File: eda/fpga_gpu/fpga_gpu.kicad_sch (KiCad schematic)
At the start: 25 parts, among them U1 ICE40HX4K-TQ144, U2 SST25VF080B-50-4x-S2Ax, U8 AMS1117-3.3, U9 AP2112K-1.2, X1 TXC-7C

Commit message: GPU routing
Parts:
- added U10: IS61C5128AL-10KLI, Package_SO:SOJ-36_10.16x23.49mm_P1.27mm, symbol Memory_RAM:IS61C5128AL-10KLI
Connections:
- net ADev0: now also U1.114 (IOT_171); no longer U1.110 (IOT_168)
- net ADev1: now also U1.113 (IOT_170); no longer U1.112 (IOT_169)
- net ADev2: now also U1.112 (IOT_169); no longer U1.113 (IOT_170)
- net ADev3: now also U1.110 (IOT_168); no longer U1.114 (IOT_171)
- net GND: now also U10.10 (GND), U10.28 (GND)
- new net: U10.27 (VDD), U10.9 (VDD)
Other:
- moved on the sheet: C10, C2, C3, C4, C5, C6, C7, C8, C9, D1, R1, R2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

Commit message: More routing on the GPU board
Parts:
- added C23: 100n, Capacitor_SMD:C_0805_2012Metric, symbol Device:C
- added H1, H2, H3, H4: MountingHole, MountingHole:MountingHole_2.5mm, symbol Mechanical:MountingHole
- added J3: programming, Connector_PinHeader_2.54mm:PinHeader_1x06_P2.54mm_Vertical, symbol Connector:Conn_01x06_Pin
- added J4: reset ground, Connector_PinHeader_2.54mm:PinHeader_1x01_P2.54mm_Vertical, symbol Connector:Conn_01x01_Pin
- added Q1: 2N7002, Package_TO_SOT_SMD:SOT-23, symbol Transistor_FET:2N7002
- added R15, R16: 10k, Resistor_SMD:R_0805_2012Metric, symbol Device:R
- D1: footprint Diode_THT:D_DO-41_SOD81_P10.16mm_Horizontal -> Diode_SMD:D_0805_2012Metric
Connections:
- net +3.3V: now also R16.2
- net Blue0: now also U1.78 (IOR_114); no longer U1.37 (IOB_56)
- net Blue1: now also U1.79 (IOR_115); no longer U1.38 (IOB_57)
- net Blue2: now also U1.80 (IOR_116); no longer U1.39 (IOB_61)
- net DIn0: now also U1.88 (IOR_137); no longer U1.73 (IOR_109)
- net DIn1: now also U1.90 (IOR_138); no longer U1.74 (IOR_110)
- net DIn2: now also U1.91 (IOR_139); no longer U1.75 (IOR_111)
- net DIn3: now also U1.93 (IOR_140_GBIN3); no longer U1.76 (IOR_112)
- net DIn4: now also U1.94 (IOR_141_GBIN2); no longer U1.78 (IOR_114)
- net DIn5: now also U1.95 (IOR_144); no longer U1.79 (IOR_115)
- net DIn6: now also U1.96 (IOR_146); no longer U1.80 (IOR_116)
- net DIn7: now also U1.97 (IOR_147); no longer U1.81 (IOR_117)
- net DOut0: now also U1.98 (IOR_148); no longer U1.82 (IOR_118)
- net DOut1: now also U1.99 (IOR_152); no longer U1.83 (IOR_119)
- net DOut2: now also U1.101 (IOR_160); no longer U1.84 (IOR_120)
- net DOut3: now also U1.102 (IOR_161); no longer U1.85 (IOR_128)
- net DOut4: now also U1.104 (IOR_164); no longer U1.87 (IOR_136)
- net DOut5: now also U1.105 (IOR_165); no longer U1.88 (IOR_137)
- net DOut6: now also U1.106 (IOR_166); no longer U1.90 (IOR_138)
- net DOut7: now also U1.107 (IOR_167); no longer U1.91 (IOR_139)
- net GND: now also C23.2, J3.2 (Pin_2), J4.1 (Pin_1), Q1.2 (S), R15.1
- net Green0: now also U1.81 (IOR_117); no longer U1.41 (IOB_63)
- net Green1: now also U1.82 (IOR_118); no longer U1.42 (IOB_64)
- net Green2: now also U1.83 (IOR_119); no longer U1.43 (IOB_71)
- net HSYNC: now also U1.75 (IOR_111); no longer U1.55 (IOB_91)
- net Red0: now also U1.84 (IOR_120); no longer U1.44 (IOB_72)
- net Red1: now also U1.85 (IOR_128); no longer U1.45 (IOB_73)
- net Red2: now also U1.87 (IOR_136); no longer U1.47 (IOB_79)
- net VCC: now also U10.27 (VDD), U10.9 (VDD), C23.1
- net VSYNC: now also U1.76 (IOR_112); no longer U1.48 (IOB_80)
- net ice40-CRESET: now also J3.1 (Pin_1), R16.1
- net ice40-SCK: now also J3.5 (Pin_5)
- net ice40-SDI: now also J3.3 (Pin_3)
- net ice40-SDO: now also J3.4 (Pin_4)
- net at R1.2, R4.2, U2.1 (~{CE}): now also J3.6 (Pin_6)
- net RamA0: now reaches U10.1 (A0)
- net RamA0: now also U1.18 (IOL_12B)
- net RamIo2: now reaches U10.11 (I/O2)
- net RamIo2: now also U1.63 (IOB_103_CBSEL0)
- net RamIo3: now reaches U10.12 (I/O3)
- net RamIo3: now also U1.64 (IOB_104_CBSEL1)
- net ~{RamWE}: now reaches U10.13 (~{WE})
- net ~{RamWE}: now also U1.44 (IOB_72)
- net RamA5: now reaches U10.14 (A5)
- net RamA5: now also U1.11 (IOL_8A)
- net RamA6: now reaches U10.15 (A6)
- net RamA6: now also U1.10 (IOL_5B)
- net RamA7: now reaches U10.16 (A7)
- net RamA7: now also U1.9 (IOL_5A)
- net RamA8: now reaches U10.17 (A8)
- net RamA8: now also U1.8 (IOL_4B)
- net RamA9: now reaches U10.18 (A9)
- net RamA9: now also U1.7 (IOL_4A)
- net RamA1: now reaches U10.2 (A1)
- net RamA1: now also U1.17 (IOL_12A)
- net RamA10: now reaches U10.20 (A10)
- net RamA10: now also U1.19 (IOL_13A)
- net RamA11: now reaches U10.21 (A11)
- net RamA11: now also U1.21 (IOL_14A_GBIN6)
- net RamA12: now reaches U10.22 (A12)
- net RamA12: now also U1.22 (IOL_14B)
- net RamA13: now reaches U10.23 (A13)
- net RamA13: now also U1.23 (IOL_17A)
- net RamA14: now reaches U10.24 (A14)
- net RamA14: now also U1.24 (IOL_17B)
- net RamIo4: now reaches U10.25 (I/O4)
- net RamIo4: now also U1.60 (IOB_95)
- net RamIo5: now reaches U10.26 (I/O5)
- net RamIo5: now also U1.56 (IOB_94)
- net RamIo6: now reaches U10.29 (I/O6)
- net RamIo6: now also U1.55 (IOB_91)
- net RamA2: now reaches U10.3 (A2)
- net RamA2: now also U1.16 (IOL_10B)
- net RamIo7: now reaches U10.30 (I/O7)
- net RamIo7: now also U1.52 (IOB_82_GBIN4)
- net ~{RamOE}: now reaches U10.31 (~{OE})
- net ~{RamOE}: now also U1.45 (IOB_73)
- net RamA15: now reaches U10.32 (A15)
- net RamA15: now also U1.25 (IOL_18A)
- net RamA16: now reaches U10.33 (A16)
- net RamA16: now also U1.29 (IOL_23B)
- net RamA17: now reaches U10.34 (A17)
- net RamA17: now also U1.31 (IOL_24A)
- net RamA18: now reaches U10.35 (A18)
- net RamA18: now also U1.32 (IOL_24B)
- net RamA3: now reaches U10.4 (A3)
- net RamA3: now also U1.15 (IOL_10A)
- net RamA4: now reaches U10.5 (A4)
- net RamA4: now also U1.12 (IOL_8B)
- net ~{RamCE}: now reaches U10.6 (~{CE})
- net ~{RamCE}: now also U1.43 (IOB_71)
- net RamIo0: now reaches U10.7 (I/O0)
- net RamIo0: now also U1.61 (IOB_96)
- net RamIo1: now reaches U10.8 (I/O1)
- net RamIo1: now also U1.62 (IOB_102)
- net FpgaIRQ: now reaches U1.128 (IOT_197_GBIN1)
- net FpgaIRQ: now also Q1.1 (G), R15.2
- new net Interfacing/~{IRQ}: Q1.3 (D)
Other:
- sheet Interfacing ports: added ~{IRQ}; removed none
- moved on the sheet: C1, C10, C19, C2, C20, C21, C22, C3, C4, C5, C6, C7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

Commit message: Update eda
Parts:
- added SW1: SW_Reset, Button_Switch_SMD:SW_SPST_TL3305A, symbol Switch:SW_Push
- added SW2: SW_FlashPwrCycle, Button_Switch_SMD:SW_SPST_TL3305A, symbol Switch:SW_Push_Open
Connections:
- net +3.3V: now also SW2.2 (B); no longer R2.2, R3.2, U2.8 (VDD)
- net GND: now also SW1.1
- net ice40-CRESET: now also SW1.2
- new net: R2.2, R3.2, SW2.1 (A), U2.8 (VDD)
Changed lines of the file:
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@@
   (junction (at 302.26 214.63) (diameter 0) (color 0 0 0 0)
   )
+  (junction (at 210.82 266.7) (diameter 0) (color 0 0 0 0)
+  )
   (junction (at 142.24 209.55) (diameter 0) (color 0 0 0 0)
   )
@@
   (junction (at 201.93 86.36) (diameter 0) (color 0 0 0 0)
   )
+  (junction (at 226.06 278.765) (diameter 0) (color 0 0 0 0)
+  )
   (junction (at 350.52 142.24) (diameter 0) (color 0 0 0 0)
   )
@@
     (stroke (width 0) (type default))
   )
+  (wire (pts (xy 232.41 194.945) (xy 232.41 196.85))
+    (stroke (width 0) (type default))
+  )
   (wire (pts (xy 350.52 71.12) (xy 386.08 71.12))
     (stroke (width 0) (type default))
@@
     (stroke (width 0) (type default))
   )
+  (wire (pts (xy 210.82 278.765) (xy 226.06 278.765))
+    (stroke (width 0) (type default))
+  )
   (wire (pts (xy 26.67 239.395) (xy 29.845 239.395))
     (stroke (width 0) (type default))
@@
     (stroke (width 0) (type default))
   )
-  (wire (pts (xy 226.06 271.78) (xy 226.06 274.32))
+  (wire (pts (xy 226.06 271.78) (xy 226.06 278.765))
     (stroke (width 0) (type default))
   )
@@
     (stroke (width 0) (type default))
   )
-  (wire (pts (xy 201.93 266.7) (xy 228.6 266.7))
+  (wire (pts (xy 201.93 266.7) (xy 210.82 266.7))
     (stroke (width 0) (type default))
   )
@@
     (stroke (width 0) (type default))
   )
+  (wire (pts (xy 210.82 266.7) (xy 228.6 266.7))
+    (stroke (width 0) (type default))
+  )
   (wire (pts (xy 56.515 252.73) (xy 56.515 251.46))
     (stroke (width 0) (type default))
@@
     (stroke (width 0) (type default))
   )
+  (wire (pts (xy 226.06 278.765) (xy 226.06 280.035))
+    (stroke (width 0) (type default))
+  )
   (wire (pts (xy 137.16 217.17) (xy 134.62 217.17))
     (stroke (width 0) (type default))
@@
     (stroke (width 0) (type default))
   )
+  (wire (pts (xy 210.82 276.86) (xy 210.82 278.765))
+    (stroke (width 0) (type default))
+  )
   (wire (pts (xy 200.66 220.98) (xy 201.93 220.98))
     (stroke (width 0) (type default))
@@
     )
   )
-  (symbol (lib_id "power:GND") (at 226.06 274.32 0) (unit 1)
-    (in_bom yes) (on_board yes) (dnp no) (fields_autoplaced)
-    (property "Reference" "#PWR046" (at 226.06 280.67 0)
+  (symbol (lib_id "power:GND") (at 226.06 280.035 0) (unit 1)
+    (in_bom yes) (on_board yes) (dnp no)
+    (property "Reference" "#PWR046" (at 226.06 286.385 0)
       (effects (font (size 1.27 1.27)) hide)
     )
-    (property "Value" "GND" (at 226.06 279.4 0)
+    (property "Value" "GND" (at 226.06 283.845 0)
       (effects (font (size 1.27 1.27)))
     )
-    (property "Footprint" "" (at 226.06 274.32 0)
+    (property "Footprint" "" (at 226.06 280.035 0)
       (effects (font (size 1.27 1.27)) hide)
     )
-    (property "Datasheet" "" (at 226.06 274.32 0)
+    (property "Datasheet" "" (at 226.06 280.035 0)
       (effects (font (size 1.27 1.27)) hide)
     )
@@
     )
   )
+  (symbol (lib_id "Switch:SW_Push") (at 210.82 271.78 90) (unit 1)
+    (in_bom yes) (on_board yes) (dnp no) (fields_autoplaced)
+    (property "Reference" "SW1" (at 212.09 271.145 90)
+      (effects (font (size 1.27 1.27)) (justify right))
+    )
+    (property "Value" "SW_Reset" (at 212.09 273.685 90)
+      (effects (font (size 1.27 1.27)) (justify right))
+    )
+    (property "Footprint" "Button_Switch_SMD:SW_SPST_TL3305A" (at 205.74 271.78 0)
+      (effects (font (size 1.27 1.27)) hide)
+    )
+    (property "Datasheet" "~" (at 205.74 271.78 0)
+      (effects (font (size 1.27 1.27)) hide)
+    )
+    (pin "1")
+    (pin "2")
+    (instances
+      (project "fpga_gpu"
+        (path "/1109c9a4-a9ef-4407-8781-29fe7740bcaf"
+          (reference "SW1") (unit 1)
+        )
+      )
+    )
+  )
   (symbol (lib_id "power:GND") (at 165.1 220.98 0) (unit 1)
     (in_bom yes) (on_board yes) (dnp no) (fields_autoplaced)
@@
     )
   )
-  (symbol (lib_id "power:+3.3V") (at 232.41 207.01 0) (unit 1)
+  (symbol (lib_id "power:+3.3V") (at 232.41 194.945 0) (unit 1)
     (in_bom yes) (on_board yes) (dnp no) (fields_autoplaced)
-    (property "Reference" "#PWR014" (at 232.41 210.82 0)
+    (property "Reference" "#PWR014" (at 232.41 198.755 0)
       (effects (font (size 1.27 1.27)) hide)
     )
-    (property "Value" "+3.3V" (at 232.41 203.2 0)
+    (property "Value" "+3.3V" (at 232.41 191.135 0)
       (effects (font (size 1.27 1.27)))
     )
-    (property "Footprint" "" (at 232.41 207.01 0)
+    (property "Footprint" "" (at 232.41 194.945 0)
       (effects (font (size 1.27 1.27)) hide)
     )
-    (property "Datasheet" "" (at 232.41 207.01 0)
+    (property "Datasheet" "" (at 232.41 194.945 0)
       (effects (font (size 1.27 1.27)) hide)
     )
@@
         )
       )
+    )
+  )
+  (symbol (lib_id "Switch:SW_Push_Open") (at 232.41 201.93 90) (unit 1)
+    (in_bom yes) (on_board yes) (dnp no) (fields_autoplaced)
+    (property "Reference" "SW2" (at 233.68 201.295 90)
+      (effects (font (size 1.27 1.27)) (justify right))
+    )
+    (property "Value" "SW_FlashPwrCycle" (at 233.68 203.835 90)
+      (effects (font (size 1.27 1.27)) (justify right))
+    )
+    (property "Footprint" "Button_Switch_SMD:SW_SPST_TL3305A" (at 227.33 201.93 0)
+      (effects (font (size 1.27 1.27)) hide)
+    )
+    (property "Datasheet" "~" (at 227.33 201.93 0)
+      (effects (font (size 1.27 1.27)) hide)
+    )
+    (pin "1")
+    (pin "2")
+    (instances
+      (project "fpga_gpu"
+        (path "/1109c9a4-a9ef-4407-8781-29fe7740bcaf"
+          (reference "SW2") (unit 1)
+        )
+      )

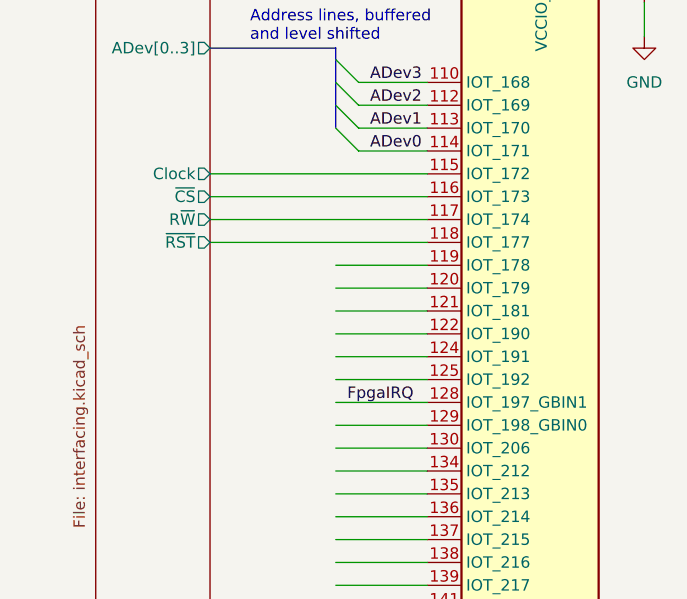
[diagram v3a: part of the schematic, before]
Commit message: Add skeleton stuff to io-card and gpu
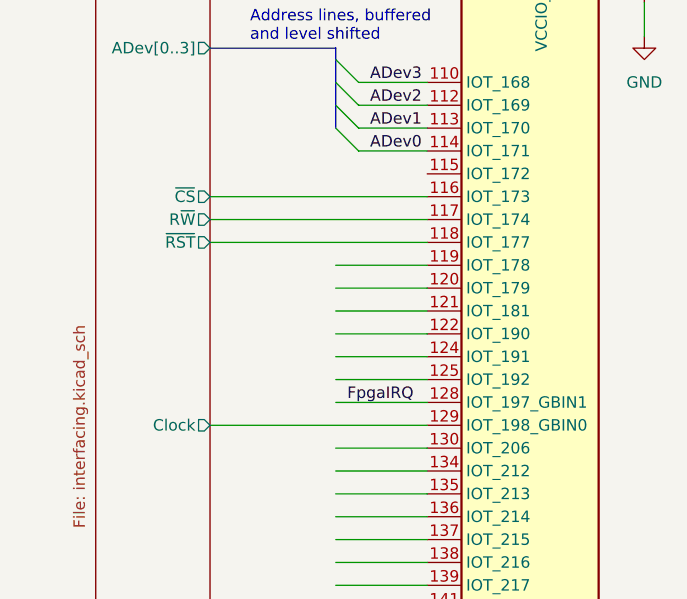
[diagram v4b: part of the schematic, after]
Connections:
- net Interfacing/Clock: now also U1.129 (IOT_198_GBIN0); no longer U1.115 (IOT_172)
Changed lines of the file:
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@@
     (stroke (width 0) (type default))
   )
-  (wire (pts (xy 59.69 119.38) (xy 69.85 119.38))
-    (stroke (width 0) (type default))
-  )
   (wire (pts (xy 264.16 88.9) (xy 274.32 88.9))
     (stroke (width 0) (type default))
@@
     (stroke (width 0) (type default))
   )
-  (wire (pts (xy 45.72 91.44) (xy 69.85 91.44))
+  (wire (pts (xy 45.72 119.38) (xy 69.85 119.38))
     (stroke (width 0) (type default))
   )
@@
       (effects (font (size 1.27 1.27)) (justify right))
     )
-    (pin "Clock" output (at 45.72 91.44 0)
+    (pin "Clock" output (at 45.72 119.38 0)
       (effects (font (size 1.27 1.27)) (justify right))
     )

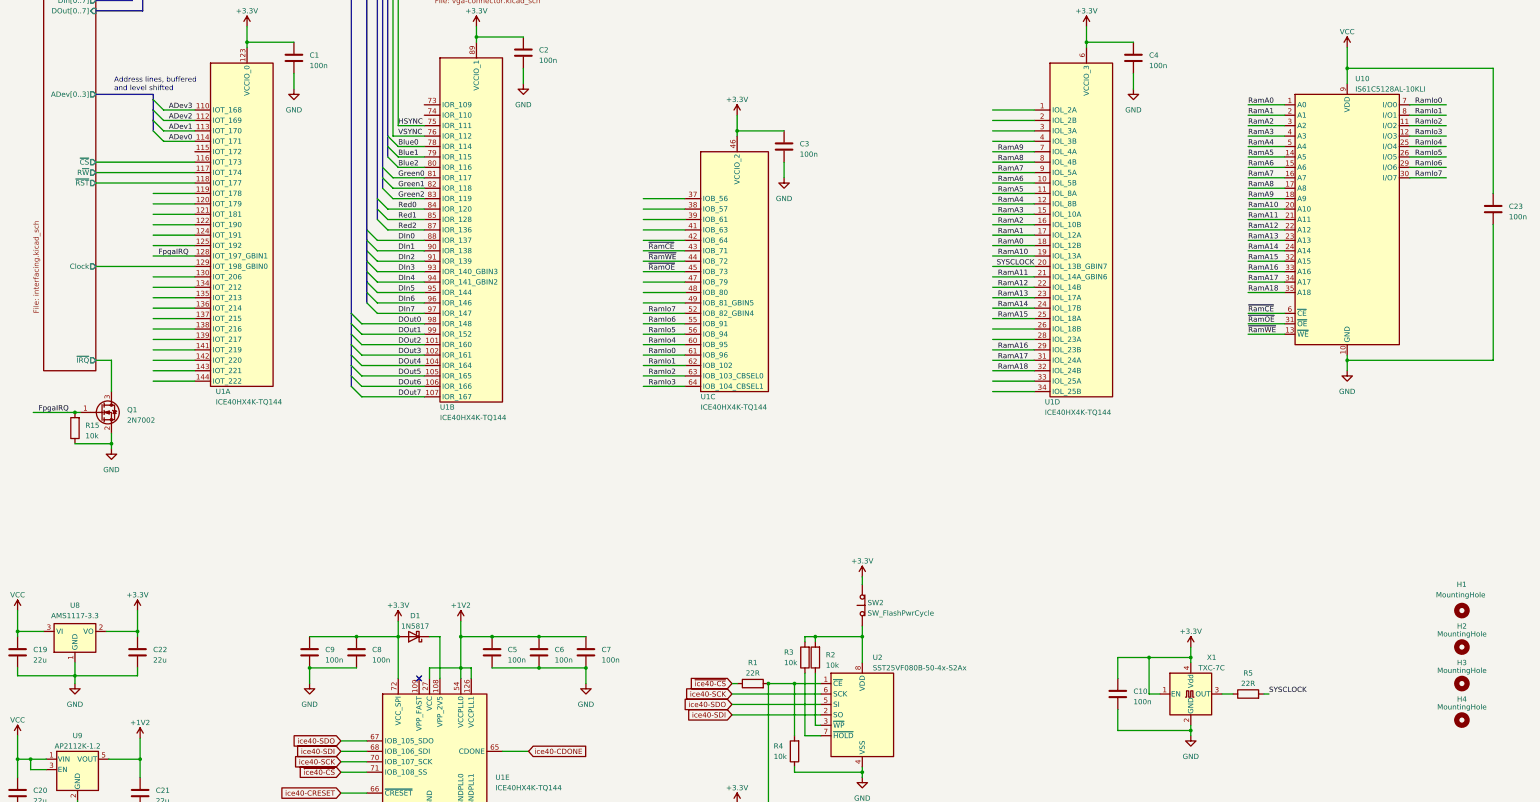
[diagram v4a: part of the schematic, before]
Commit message: Add expansion backplane
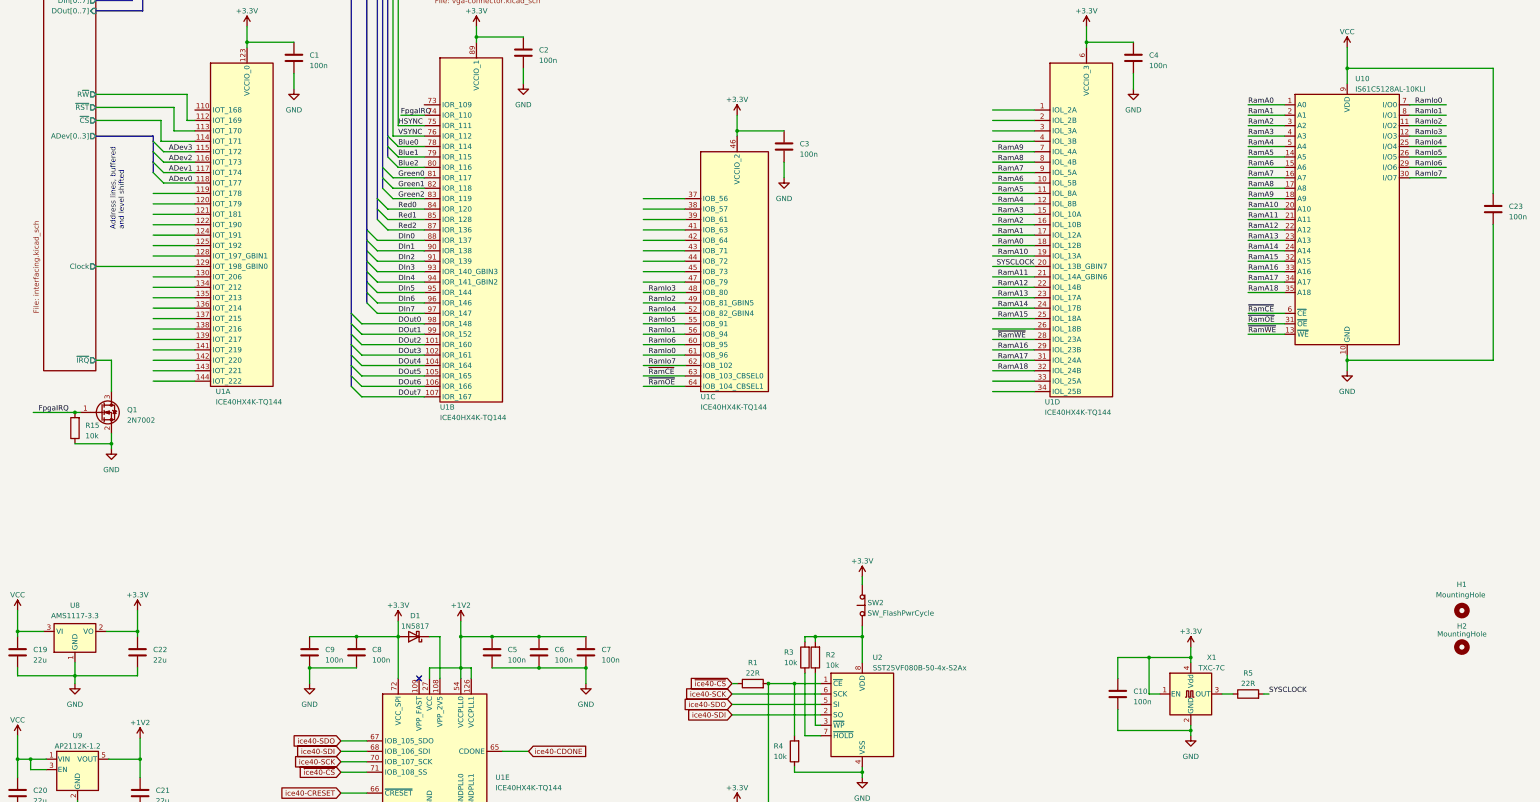
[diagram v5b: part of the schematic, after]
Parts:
- removed H3, H4: MountingHole, MountingHole:MountingHole_2.5mm, symbol Mechanical:MountingHole
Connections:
- net ADev0: now also U1.118 (IOT_177); no longer U1.114 (IOT_171)
- net ADev1: now also U1.117 (IOT_174); no longer U1.113 (IOT_170)
- net ADev2: now also U1.116 (IOT_173); no longer U1.112 (IOT_169)
- net ADev3: now also U1.115 (IOT_172); no longer U1.110 (IOT_168)
- net FpgaIRQ: now also U1.74 (IOR_110); no longer U1.128 (IOT_197_GBIN1)
- net Interfacing/R~{W}: now also U1.112 (IOT_169); no longer U1.117 (IOT_174)
- net Interfacing/~{CS}: now also U1.114 (IOT_171); no longer U1.116 (IOT_173)
- net Interfacing/~{RST}: now also U1.113 (IOT_170); no longer U1.118 (IOT_177)
- net RamIo1: now also U1.56 (IOB_94); no longer U1.62 (IOB_102)
- net RamIo2: now also U1.49 (IOB_81_GBIN5); no longer U1.63 (IOB_103_CBSEL0)
- net RamIo3: now also U1.48 (IOB_80); no longer U1.64 (IOB_104_CBSEL1)
- net RamIo4: now also U1.52 (IOB_82_GBIN4); no longer U1.60 (IOB_95)
- net RamIo5: now also U1.55 (IOB_91); no longer U1.56 (IOB_94)
- net RamIo6: now also U1.60 (IOB_95); no longer U1.55 (IOB_91)
- net RamIo7: now also U1.62 (IOB_102); no longer U1.52 (IOB_82_GBIN4)
- net ~{RamCE}: now also U1.63 (IOB_103_CBSEL0); no longer U1.43 (IOB_71)
- net ~{RamOE}: now also U1.64 (IOB_104_CBSEL1); no longer U1.45 (IOB_73)
- net ~{RamWE}: now also U1.28 (IOL_23A); no longer U1.44 (IOB_72)
